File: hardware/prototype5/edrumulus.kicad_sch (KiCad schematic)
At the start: 94 parts, among them J1 Trigger Connector, J2 Raspberry Pi GPIO pins, U1 ESP32-WROOM-32U, U2 AMS1117-3.3, U3 MCP1754S-3302xMB

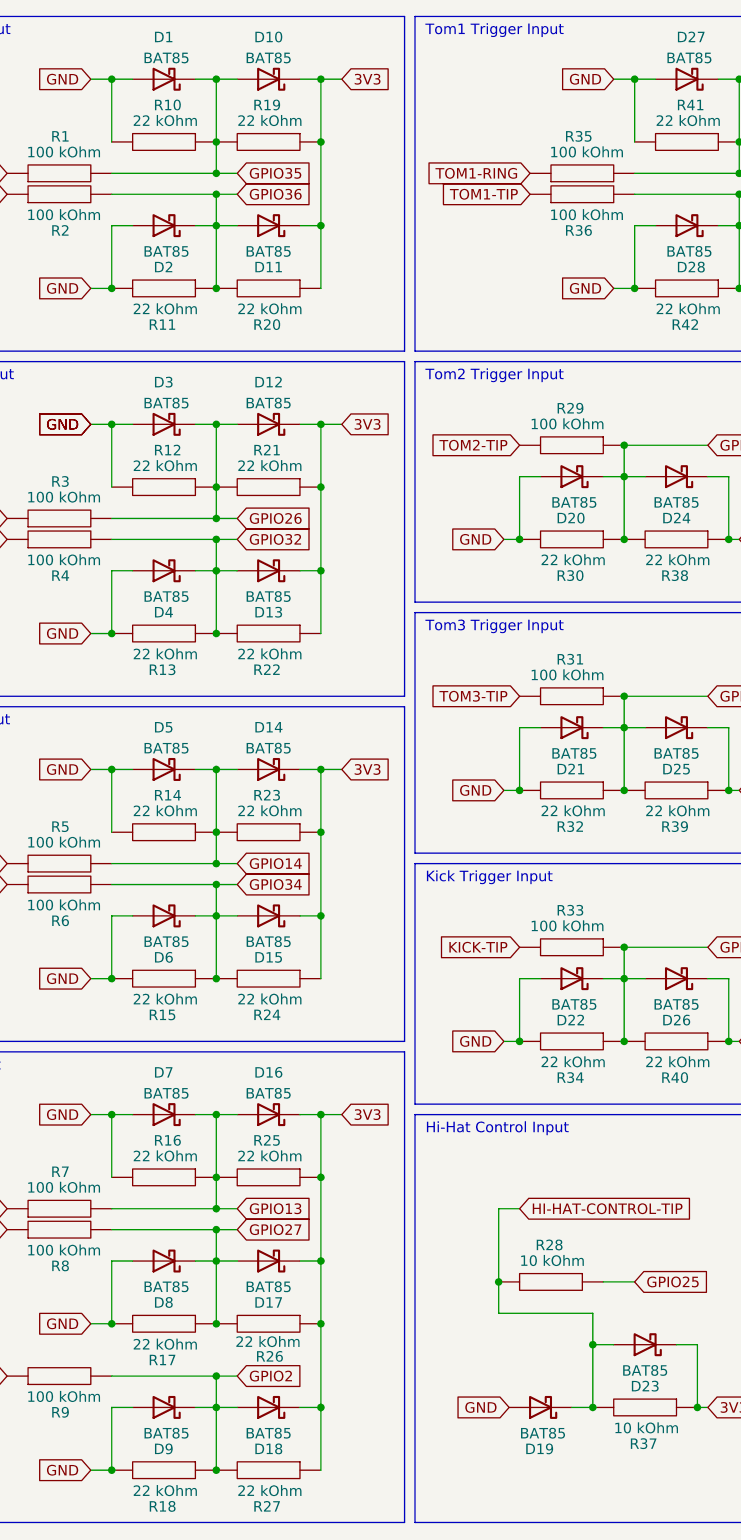
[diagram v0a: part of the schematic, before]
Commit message: fix annotations and other problems in prototype 5
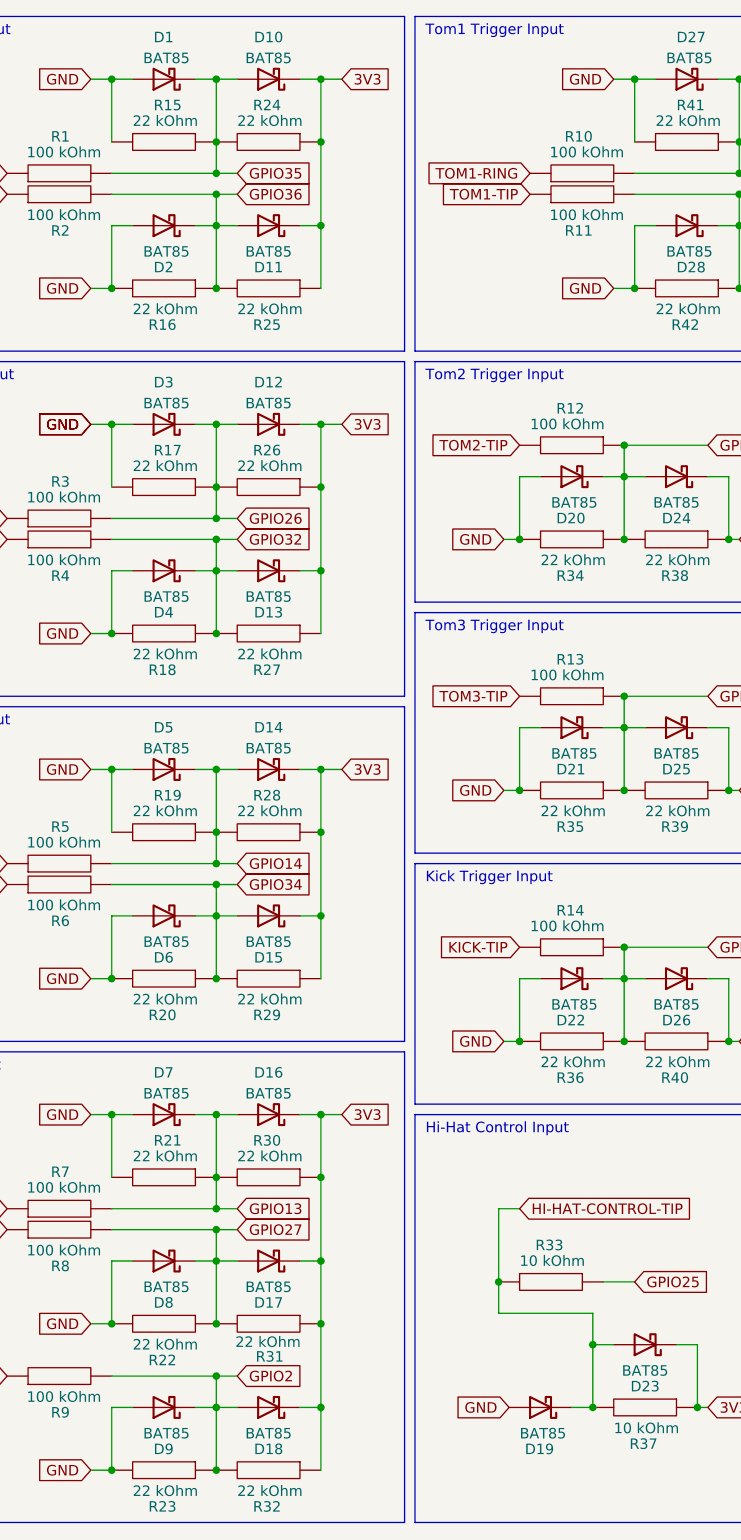
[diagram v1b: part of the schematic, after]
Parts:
- renumbered R35 to R10, R36 to R11, R29 to R12, R31 to R13, R33 to R14, R10 to R15, R11 to R16, R12 to R17, R13 to R18, R14 to R19, R15 to R20, R16 to R21, R17 to R22, R18 to R23, R19 to R24, R20 to R25, R21 to R26, R22 to R27, R23 to R28, R24 to R29, R25 to R30, R26 to R31, R27 to R32, R28 to R33, R30 to R34, R32 to R35, R34 to R36

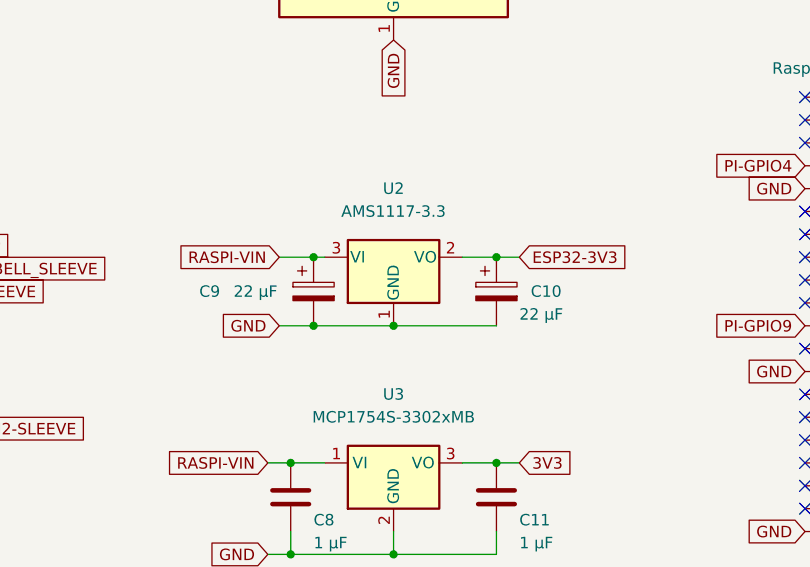
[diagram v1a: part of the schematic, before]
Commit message: use larger size for caps
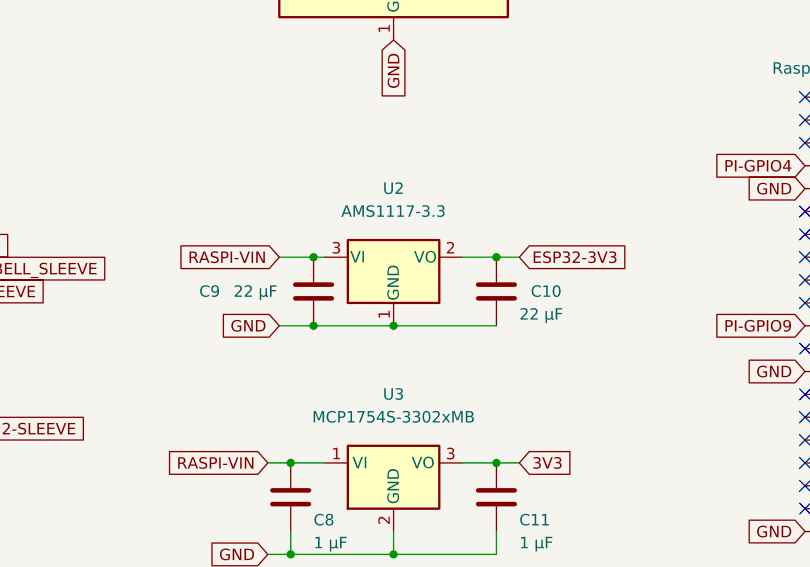
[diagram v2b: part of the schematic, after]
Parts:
- C10, C9: footprint Capacitor_SMD:C_1206_3216Metric_Pad1.33x1.80mm_HandSolder -> Capacitor_SMD:C_1210_3225Metric_Pad1.33x2.70mm_HandSolder; symbol Device:C_Polarized -> Device:C
- C11, C8: footprint Capacitor_SMD:C_1206_3216Metric_Pad1.33x1.80mm_HandSolder -> Capacitor_SMD:C_1210_3225Metric_Pad1.33x2.70mm_HandSolder
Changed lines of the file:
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@@
       (effects (font (size 1.27 1.27)) (justify left))
     )
-    (property "Footprint" "Capacitor_SMD:C_1206_3216Metric_Pad1.33x1.80mm_HandSolder" (id 2) (at 218.1352 157.48 0)
+    (property "Footprint" "Capacitor_SMD:C_1210_3225Metric_Pad1.33x2.70mm_HandSolder" (id 2) (at 218.1352 157.48 0)
       (effects (font (size 1.27 1.27)) hide)
     )
@@
     (pin "2")
   )
-  (symbol (lib_id "Device:C_Polarized") (at 196.85 130.81 0) (unit 1)
+  (symbol (lib_id "Device:C") (at 196.85 130.81 0) (unit 1)
     (in_bom yes) (on_board yes)
     (property "Reference" "C9" (id 0) (at 184.15 130.81 0)
@@
       (effects (font (size 1.27 1.27)) (justify left))
     )
-    (property "Footprint" "Capacitor_SMD:C_1206_3216Metric_Pad1.33x1.80mm_HandSolder" (id 2) (at 197.8152 134.62 0)
+    (property "Footprint" "Capacitor_SMD:C_1210_3225Metric_Pad1.33x2.70mm_HandSolder" (id 2) (at 197.8152 134.62 0)
       (effects (font (size 1.27 1.27)) hide)
     )
@@
       (effects (font (size 1.27 1.27)) (justify left))
     )
-    (property "Footprint" "Capacitor_SMD:C_1206_3216Metric_Pad1.33x1.80mm_HandSolder" (id 2) (at 195.2752 157.48 0)
+    (property "Footprint" "Capacitor_SMD:C_1210_3225Metric_Pad1.33x2.70mm_HandSolder" (id 2) (at 195.2752 157.48 0)
       (effects (font (size 1.27 1.27)) hide)
     )
@@
     (pin "2")
   )
-  (symbol (lib_id "Device:C_Polarized") (at 217.17 130.81 0) (unit 1)
+  (symbol (lib_id "Device:C") (at 217.17 130.81 0) (unit 1)
     (in_bom yes) (on_board yes)
     (property "Reference" "C10" (id 0) (at 220.98 130.81 0)
@@
       (effects (font (size 1.27 1.27)) (justify left))
     )
-    (property "Footprint" "Capacitor_SMD:C_1206_3216Metric_Pad1.33x1.80mm_HandSolder" (id 2) (at 218.1352 134.62 0)
+    (property "Footprint" "Capacitor_SMD:C_1210_3225Metric_Pad1.33x2.70mm_HandSolder" (id 2) (at 218.1352 134.62 0)
       (effects (font (size 1.27 1.27)) hide)
     )
@@
     )
     (path "/d0b85be4-288a-40b2-aed1-c5f115253616"
-      (reference "C8") (unit 1) (value "1 µF") (footprint "Capacitor_SMD:C_1206_3216Metric_Pad1.33x1.80mm_HandSolder")
+      (reference "C8") (unit 1) (value "1 µF") (footprint "Capacitor_SMD:C_1210_3225Metric_Pad1.33x2.70mm_HandSolder")
     )
     (path "/b0ddc1b3-5b62-412d-a8b0-6e4af226aff4"
-      (reference "C9") (unit 1) (value "22 µF") (footprint "Capacitor_SMD:C_1206_3216Metric_Pad1.33x1.80mm_HandSolder")
+      (reference "C9") (unit 1) (value "22 µF") (footprint "Capacitor_SMD:C_1210_3225Metric_Pad1.33x2.70mm_HandSolder")
     )
     (path "/f4138a22-f212-4224-b9f1-314577e7e9c7"
-      (reference "C10") (unit 1) (value "22 µF") (footprint "Capacitor_SMD:C_1206_3216Metric_Pad1.33x1.80mm_HandSolder")
+      (reference "C10") (unit 1) (value "22 µF") (footprint "Capacitor_SMD:C_1210_3225Metric_Pad1.33x2.70mm_HandSolder")
     )
     (path "/825167af-630d-44f2-820a-b123101d3414"
-      (reference "C11") (unit 1) (value "1 µF") (footprint "Capacitor_SMD:C_1206_3216Metric_Pad1.33x1.80mm_HandSolder")
+      (reference "C11") (unit 1) (value "1 µF") (footprint "Capacitor_SMD:C_1210_3225Metric_Pad1.33x2.70mm_HandSolder")
     )
     (path "/00000000-0000-0000-0000-000061bffa85"

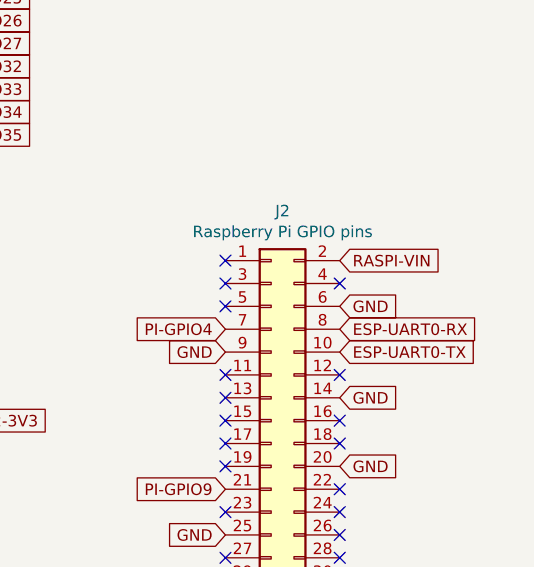
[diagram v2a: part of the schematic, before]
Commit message: move the ESP32 unit
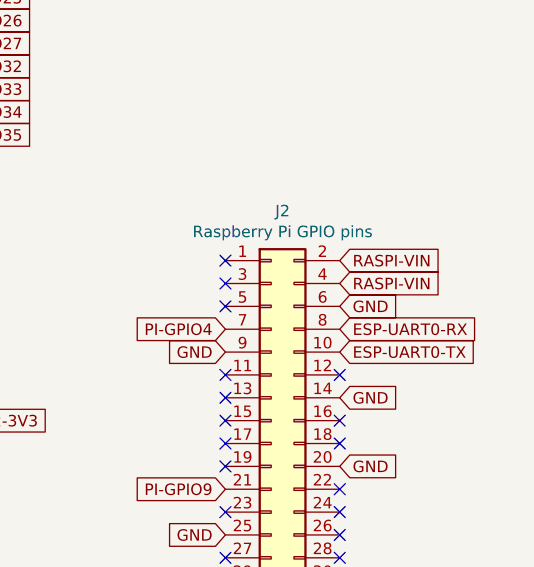
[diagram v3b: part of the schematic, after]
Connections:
- net RASPI-VIN: now also J2.4 (Pin_4)
- no-connect marks 43 -> 42
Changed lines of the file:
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@@
   (no_connect (at 251.46 127))
   (no_connect (at 251.46 124.46))
-  (no_connect (at 264.16 111.76))
   (no_connect (at 251.46 154.94))
   (no_connect (at 142.24 148.59))
@@
     )
   )
+  (global_label "RASPI-VIN" (shape input) (at 264.16 111.76 0) (fields_autoplaced)
+    (effects (font (size 1.27 1.27)) (justify left))
+    (property "Referenzen zwischen Schaltplänen" "${INTERSHEET_REFS}" (id 0) (at 276.5232 111.6806 0)
+      (effects (font (size 1.27 1.27)) (justify left) hide)
+    )
+  )

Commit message: change resistor size from 1206 to 0603 for prototype 5
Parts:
- R1, R10, R11, R12, R13, R14, R15, R16, R17, R18, R19, R2, R20, R21, R22, R23, R24, R25, R26, R27, R28, R29, R3, R30, R31, R32, R33, R34, R35, R36, R37, R38, R39, R4, R40, R41, R42, R43, R44, R45, R46, R47, R5, R6, R7, R8, R9: footprint Resistor_SMD:R_1206_3216Metric_Pad1.30x1.75mm_HandSolder -> Resistor_SMD:R_0603_1608Metric_Pad0.98x0.95mm_HandSolder

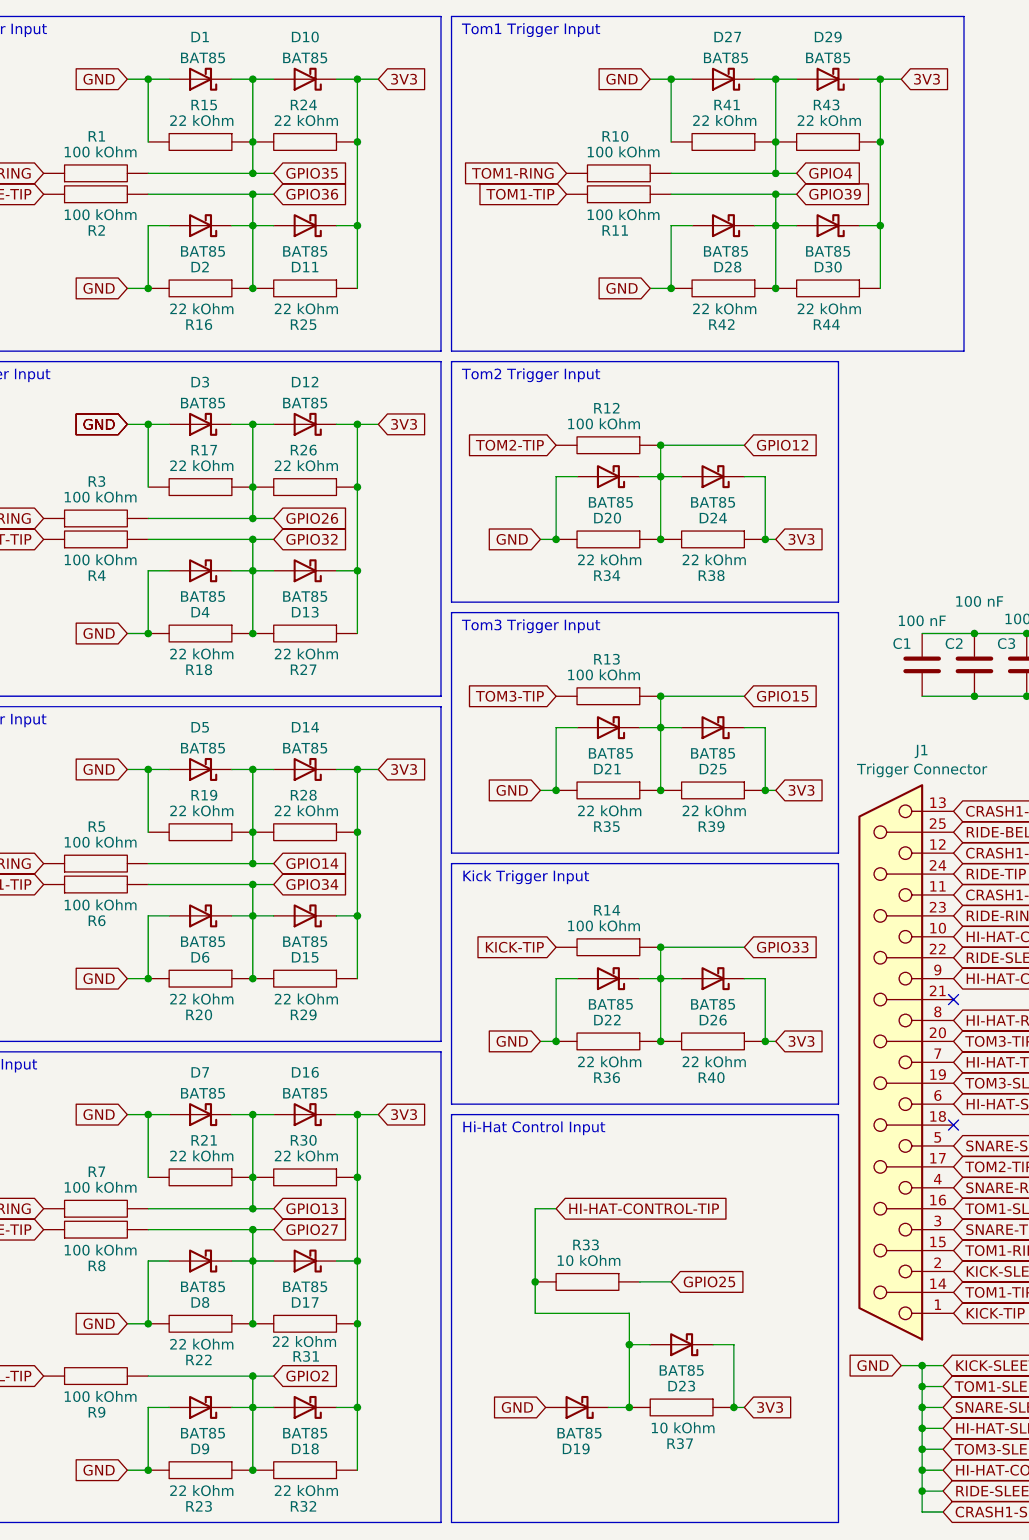
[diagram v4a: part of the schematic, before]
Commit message: use BAV99 instead of BAT85 diodes
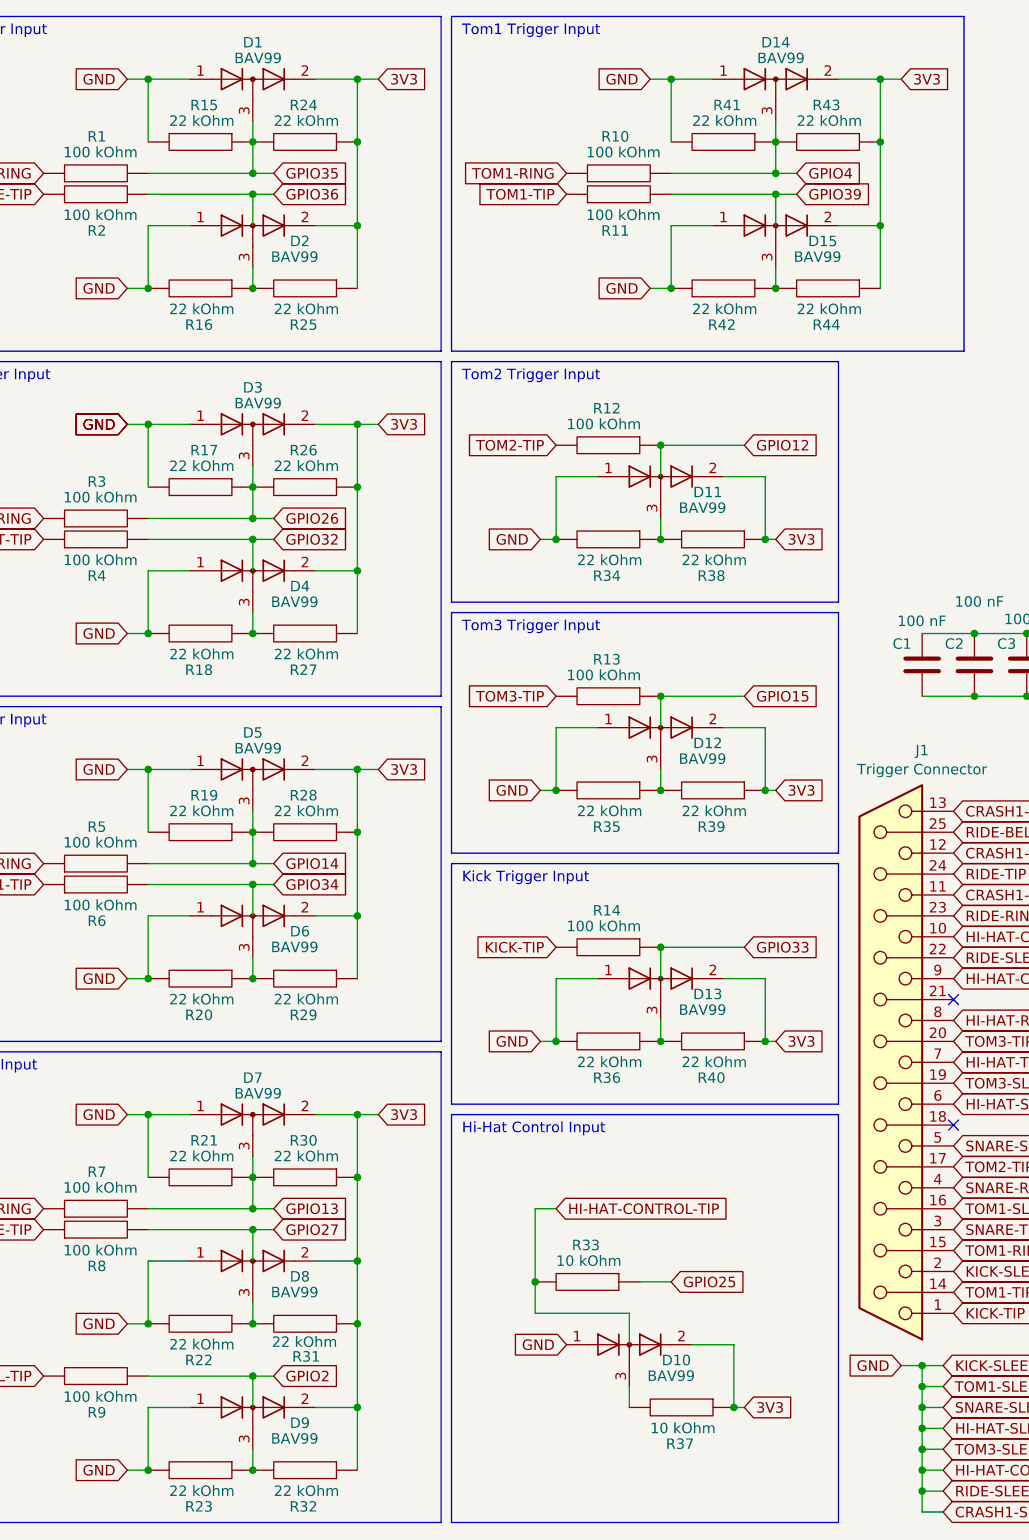
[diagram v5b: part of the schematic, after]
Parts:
- removed D1, D10, D11, D12, D13, D14, D15, D16, D17, D18, D19, D2, D20, D21, D22, D23, D24, D25, D26, D27, D28, D29, D3, D30, D4, D5, D6, D7, D8, D9: BAT85, Diode_SMD:D_MiniMELF, symbol Diode:BAT85
- added D1, D10, D11, D12, D13, D14, D15, D2, D3, D4, D5, D6, D7, D8, D9: BAV99, Package_TO_SOT_SMD:SOT-23, symbol Diode:BAV99
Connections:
- net 3V3: now also D1.2 (A), D10.2 (A), D11.2 (A), D12.2 (A), D13.2 (A), D14.2 (A), D15.2 (A), D2.2 (A), D3.2 (A), D4.2 (A), D5.2 (A), D6.2 (A), D7.2 (A), D8.2 (A), D9.2 (A)
- net CRASH1-SLEEVE: now also D1.1 (K), D10.1 (K), D11.1 (K), D12.1 (K), D13.1 (K), D14.1 (K), D15.1 (K), D2.1 (K), D3.1 (K), D4.1 (K), D5.1 (K), D6.1 (K), D7.1 (K), D8.1 (K), D9.1 (K)
- net GPIO12: no longer R34.1, R38.2
- net GPIO13: now also D7.3 (K)
- net GPIO14: now also D5.3 (K)
- net GPIO15: no longer R35.1, R39.2
- net GPIO2: no longer R23.1, R32.2
- net GPIO26: now also D3.3 (K)
- net GPIO27: no longer R22.1, R31.2
- net GPIO32: no longer R18.1, R27.2
- net GPIO33: no longer R36.1, R40.2
- net GPIO34: no longer R20.1, R29.2
- net GPIO35: now also D1.3 (K)
- net GPIO36: no longer R16.1, R25.2
- net GPIO39: no longer R42.1, R44.2
- net GPIO4: now also D14.3 (K)
- net HI-HAT-CONTROL-TIP: no longer R37.2
- new net: D2.3 (K), R16.1, R25.2
- new net: D13.3 (K), R36.1, R40.2
- new net: D4.3 (K), R18.1, R27.2
- new net: D10.3 (K), R37.2
- new net: D6.3 (K), R20.1, R29.2
- new net: D8.3 (K), R22.1, R31.2
- new net: D11.3 (K), R34.1, R38.2
- new net: D9.3 (K), R23.1, R32.2
- new net: D12.3 (K), R35.1, R39.2
- new net: D15.3 (K), R42.1, R44.2
